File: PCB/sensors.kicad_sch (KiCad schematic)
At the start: 0 parts

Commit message: Added more components and added most needed values for the nrf example schematic
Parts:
- added J3: AudioJack4, symbol Connector_Audio:AudioJack4
- added U4: LTR-303ALS-01, OptoDevice:Lite-On_LTR-303ALS-01, symbol Sensor_Optical:LTR-303ALS-01
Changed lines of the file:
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@@
 	(generator_version "8.0")
 	(paper "A4")
+	(global_label "P0.07_EN_SENSOR_BUS"
+		(shape input)
+		(at 115.57 76.2 0)
+		(fields_autoplaced yes)
+		(effects
+			(font
+				(size 1.27 1.27)
+			)
+			(justify left)
+		)
+		(property "Intersheetrefs" "${INTERSHEET_REFS}"
+			(at 140.7498 76.2 0)
+			(effects
+				(font
+					(size 1.27 1.27)
+				)
+				(justify left)
+				(hide yes)
+			)
+		)
+	)
+	(global_label "P0.14_SCL"
+		(shape input)
+		(at 115.57 81.28 0)
+		(fields_autoplaced yes)
+		(effects
+			(font
+				(size 1.27 1.27)
+			)
+			(justify left)
+		)
+		(property "Intersheetrefs" "${INTERSHEET_REFS}"
+			(at 128.5337 81.28 0)
+			(effects
+				(font
+					(size 1.27 1.27)
+				)
+				(justify left)
+				(hide yes)
+			)
+		)
+	)
+	(global_label "P0.15_SDA"
+		(shape input)
+		(at 115.57 83.82 0)
+		(fields_autoplaced yes)
+		(effects
+			(font
+				(size 1.27 1.27)
+			)
+			(justify left)
+		)
+		(property "Intersheetrefs" "${INTERSHEET_REFS}"
+			(at 128.5942 83.82 0)
+			(effects
+				(font
+					(size 1.27 1.27)
+				)
+				(justify left)
+				(hide yes)
+			)
+		)
+	)
+	(symbol
+		(lib_id "Sensor_Optical:LTR-303ALS-01")
+		(at 203.2 91.44 0)
+		(unit 1)
+		(exclude_from_sim no)
+		(in_bom yes)
+		(on_board yes)
+		(dnp no)
+		(fields_autoplaced yes)
+		(property "Reference" "U4"
+			(at 219.71 85.1214 0)
+			(effects
+				(font
+					(size 1.27 1.27)
+				)
+			)
+		)
+		(property "Value" "LTR-303ALS-01"
+			(at 219.71 87.6614 0)
+			(effects
+				(font
+					(size 1.27 1.27)
+				)
+			)
+		)
+		(property "Footprint" "OptoDevice:Lite-On_LTR-303ALS-01"
+			(at 203.2 80.01 0)
+			(effects
+				(font
+					(size 1.27 1.27)
+				)
+				(hide yes)
+			)
+		)
+		(property "Datasheet" "https://optoelectronics.liteon.com/upload/download/DS86-2013-0004/LTR-303ALS-01_DS_V1.pdf"
+			(at 195.58 82.55 0)
+			(effects
+				(font
+					(size 1.27 1.27)
+				)
+				(hide yes)
+			)
+		)
+		(property "Description" "ambient light sensor, i2c interface, 0.01 to 64k lux, 2.4-3.6V"
+			(at 203.2 91.44 0)
+			(effects
+				(font
+					(size 1.27 1.27)
+				)
+				(hide yes)
+			)
+		)
+		(pin "1"
+		)
+		(pin "3"
+		)
+		(pin "4"
+		)
+		(pin "5"
+		)
+		(pin "6"
+		)
+		(pin "2"
+		)
+		(instances
+			(project "Plant_Thing"
+				(path "/3604ffe7-6852-4862-a71a-75c04c0147cb/38766e62-e2f9-438f-aa7f-b6d1382d0577"
+					(reference "U4")
+					(unit 1)
+				)
+			)
+		)
+	)
+	(symbol
+		(lib_id "Connector_Audio:AudioJack4")
+		(at 50.8 45.72 0)
+		(unit 1)
+		(exclude_from_sim no)
+		(in_bom yes)
+		(on_board yes)
+		(dnp no)
+		(fields_autoplaced yes)
+		(property "Reference" "J3"
+			(at 48.26 36.83 0)
+			(effects
+				(font
+					(size 1.27 1.27)
+				)
+			)
+		)
+		(property "Value" "AudioJack4"
+			(at 48.26 39.37 0)
+			(effects
+				(font
+					(size 1.27 1.27)
+				)
+			)
+		)
+		(property "Footprint" ""
+			(at 50.8 45.72 0)
+			(effects
+				(font
+					(size 1.27 1.27)
+				)
+				(hide yes)
+			)
+		)
+		(property "Datasheet" "~"
+			(at 50.8 45.72 0)
+			(effects
+				(font
+					(size 1.27 1.27)
+				)
+				(hide yes)
+			)
+		)
+		(property "Description" "Audio Jack, 4 Poles (TRRS)"
+			(at 50.8 45.72 0)
+			(effects
+				(font
+					(size 1.27 1.27)
+				)
+				(hide yes)
+			)
+		)
+		(pin "R1"
+		)
+		(pin "T"
+		)
+		(pin "S"
+		)
+		(pin "R2"
+		)
+		(instances
+			(project "Plant_Thing"
+				(path "/3604ffe7-6852-4862-a71a-75c04c0147cb/38766e62-e2f9-438f-aa7f-b6d1382d0577"
+					(reference "J3")
+					(unit 1)
+				)
+			)
+		)
+	)
 )

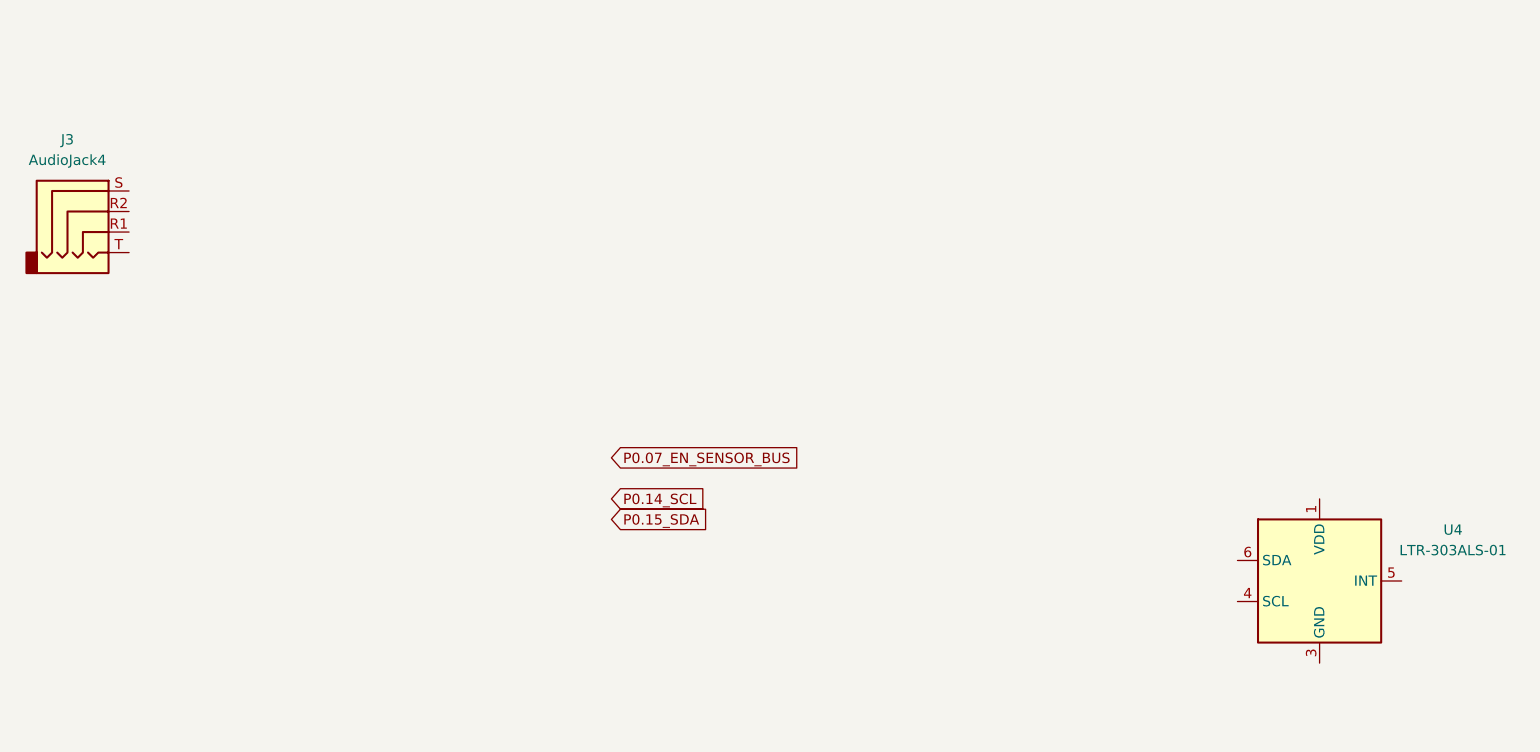
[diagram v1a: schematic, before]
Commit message: Added the Calathea Leaf as the outline and artwork for the project
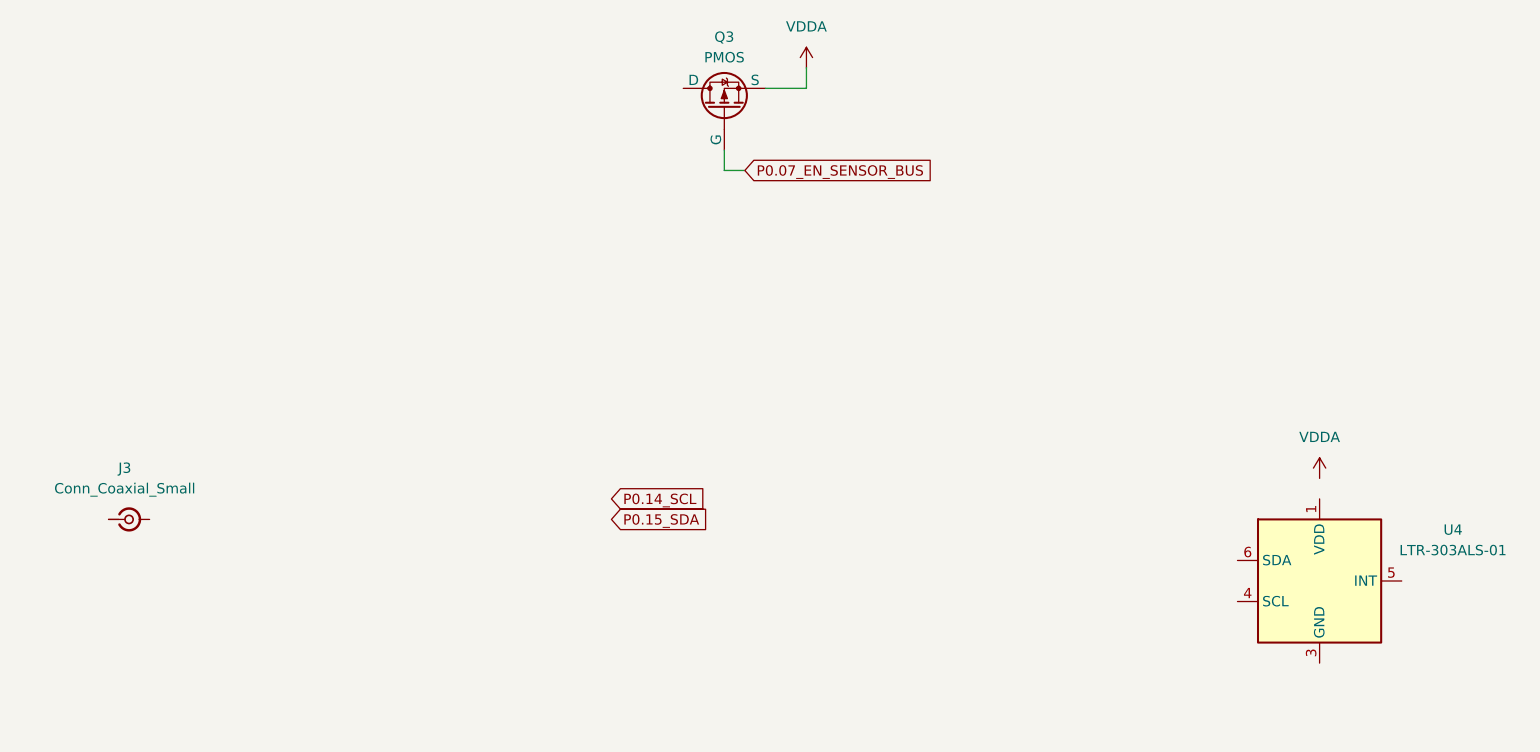
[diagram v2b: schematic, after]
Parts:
- removed J3: AudioJack4, symbol Connector_Audio:AudioJack4
- added J3: Conn_Coaxial_Small, Connector_Coaxial:SMA_Amphenol_132289_EdgeMount, symbol Connector:Conn_Coaxial_Small
- added Q3: PMOS, symbol Simulation_SPICE:PMOS
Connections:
- net P0.07_EN_SENSOR_BUS: now also Q3.2 (G)
- new net VDDA: Q3.3 (S)

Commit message: added dcdc for external components. Changed board edge to a rect for easier dev board routuing.
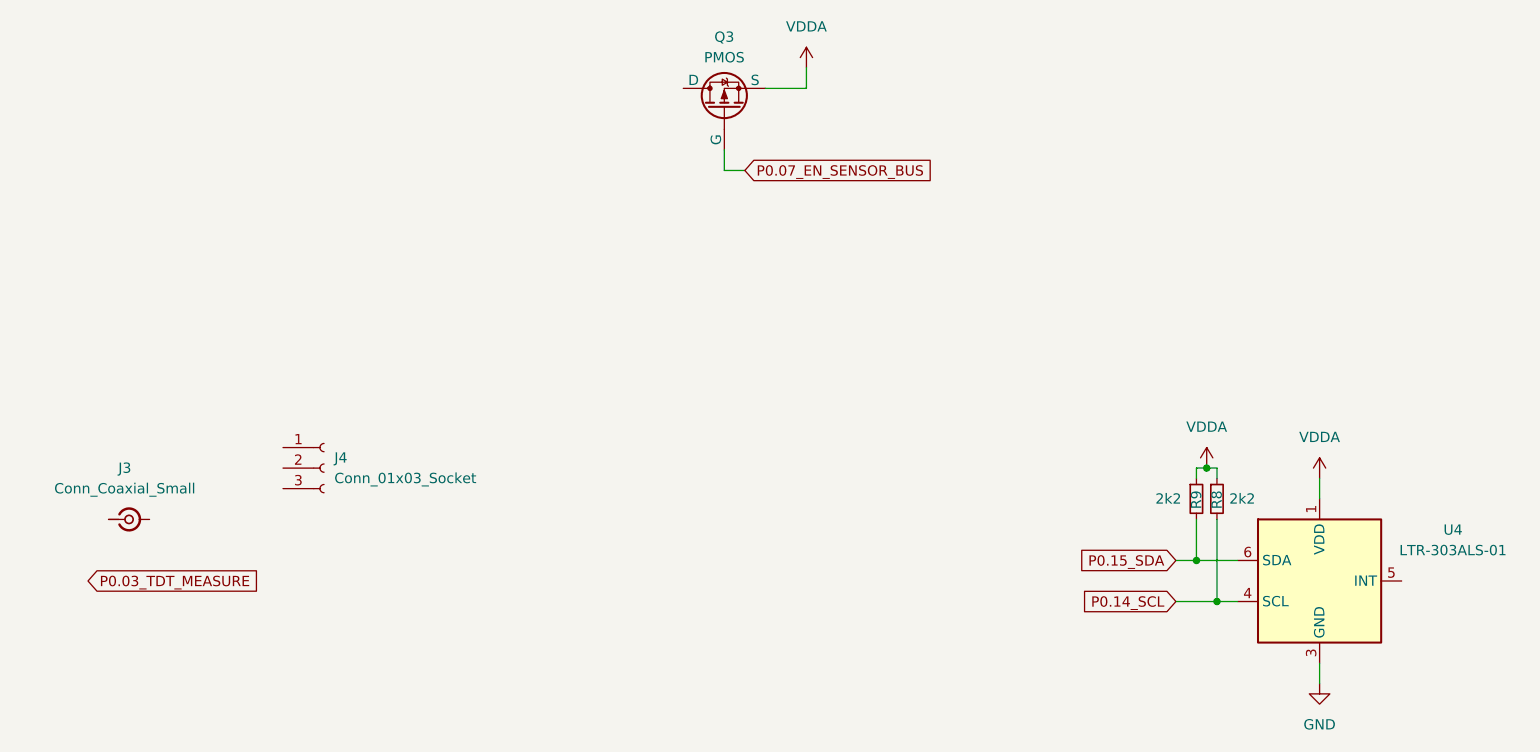
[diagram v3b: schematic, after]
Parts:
- added J4: Conn_01x03_Socket, Connector_PinSocket_2.54mm:PinSocket_1x03_P2.54mm_Horizontal, symbol Connector:Conn_01x03_Socket
- added R8, R9: 2k2, Resistor_SMD:R_0402_1005Metric, symbol Device:R_Small
- J3: footprint Connector_Coaxial:SMA_Amphenol_132289_EdgeMount -> Connector_Coaxial:U.FL_Molex_MCRF_73412-0110_Vertical
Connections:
- net P0.14_SCL: now also U4.4 (SCL), R8.2
- net P0.15_SDA: now also U4.6 (SDA), R9.2
- net VDDA: now also U4.1 (VDD), R8.1, R9.1
- net GND: now reaches U4.3 (GND)

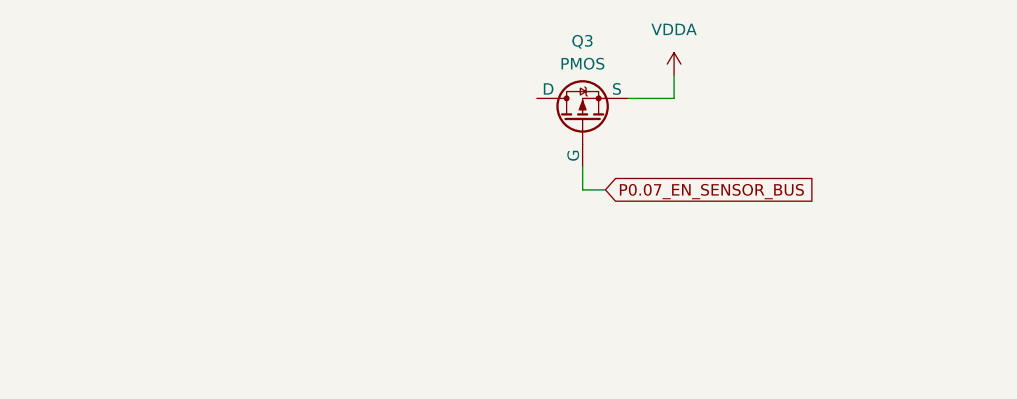
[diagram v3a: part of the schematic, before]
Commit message: redid the pcb layout for a more bigger devboard approach. Added a few more components and the antenna.
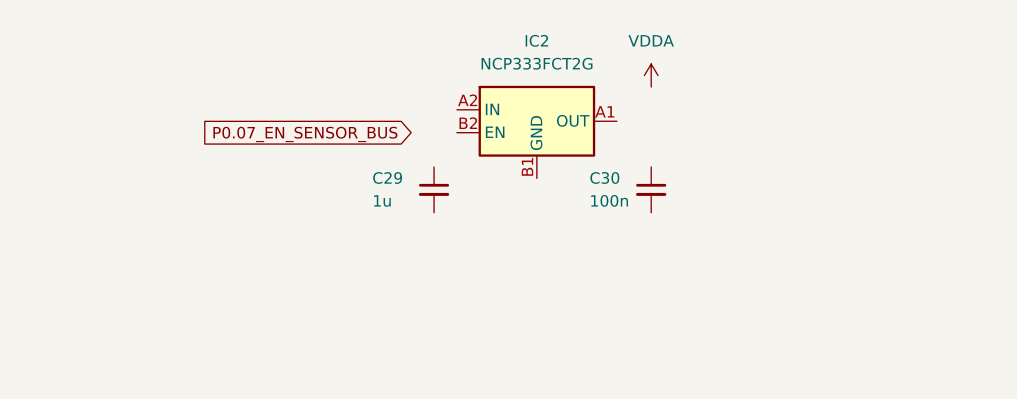
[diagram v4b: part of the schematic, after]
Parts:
- removed Q3: PMOS, symbol Simulation_SPICE:PMOS
- added C29: 1u, Capacitor_SMD:C_0402_1005Metric, symbol Device:C_Small
- added C30: 100n, Capacitor_SMD:C_0402_1005Metric, symbol Device:C_Small
- added IC2: NCP333FCT2G, BGA4C40P2X2_76X76X63, symbol NCP333FCT2G:NCP333FCT2G

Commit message: Added more Components
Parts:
- added J6: TDT, Connector_PinHeader_2.54mm:PinHeader_1x02_P2.54mm_Vertical, symbol Connector:Conn_01x02_Pin
- added TP13, TP3, TP4: TestPoint_Small, TestPoint:TestPoint_Pad_D1.0mm, symbol Connector:TestPoint_Small
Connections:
- net GND: now also C29.2, C30.2, IC2.B1 (GND)
- net P0.07_EN_SENSOR_BUS: now also IC2.B2 (EN)
- net P0.14_SCL: now also TP3.1
- net P0.15_SDA: now also TP4.1
- net VDDA: now also C30.1, IC2.A1 (OUT)
- net at U4.5 (INT): now also TP13.1
- net +3.3V: now reaches IC2.A2 (IN)
- net +3.3V: now also C29.1
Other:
- moved on the sheet: C30

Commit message: Continued on Devboard
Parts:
- removed J3: Conn_Coaxial_Small, Connector_Coaxial:U.FL_Molex_MCRF_73412-0110_Vertical, symbol Connector:Conn_Coaxial_Small
- removed J4: Conn_01x03_Socket, Connector_PinSocket_2.54mm:PinSocket_1x03_P2.54mm_Horizontal, symbol Connector:Conn_01x03_Socket
- added J3: Conn_01x06_Pin, Connector_PinHeader_2.54mm:PinHeader_1x06_P2.54mm_Vertical, symbol Connector:Conn_01x06_Pin
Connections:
- net GND: now also J3.1 (Pin_1), J3.3 (Pin_3), J3.5 (Pin_5)
- net P0.03_TDT_MEASURE: now also J3.2 (Pin_2)
- net P0.04_AGPIO: now also J3.4 (Pin_4)
- net VDDA: now also J6.1 (Pin_1)
- net at J6.2 (Pin_2): now also J3.6 (Pin_6)
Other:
- moved on the sheet: J6

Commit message: Finished Devboard
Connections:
- net GND: no longer J3.3 (Pin_3)
- net P0.04_AGPIO renamed P0.05_AIN3
- new net P0.04_AIN2: J3.3 (Pin_3)
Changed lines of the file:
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@@
+		)
+	)
+	(global_label "P0.04_AIN2"
+		(shape input)
+		(at 92.71 95.25 0)
+		(fields_autoplaced yes)
+		(effects
+			(font
+				(size 1.27 1.27)
+			)
+			(justify left)
+		)
+		(property "Intersheetrefs" "${INTERSHEET_REFS}"
+			(at 106.3995 95.25 0)
+			(effects
+				(font
+					(size 1.27 1.27)
+				)
+				(justify left)
+				(hide yes)
+			)
 		)
 	)
@@
 		)
 	)
-	(global_label "P0.04_AGPIO"
+	(global_label "P0.05_AIN3"
 		(shape input)
 		(at 92.71 92.71 0)
@@
 		)
 		(property "Intersheetrefs" "${INTERSHEET_REFS}"
-			(at 107.73 92.71 0)
+			(at 106.3995 92.71 0)
 			(effects
 				(font
@@
 					(unit 1)
 				)
-			)
-		)
-	)
-	(symbol
-		(lib_id "power:GND")
-		(at 92.71 95.25 90)
-		(mirror x)
-		(unit 1)
-		(exclude_from_sim no)
-		(in_bom yes)
-		(on_board yes)
-		(dnp no)
-		(fields_autoplaced yes)
-		(property "Reference" "#PWR070"
-			(at 99.06 95.25 0)
-			(effects
-				(font
-					(size 1.27 1.27)
-				)
-				(hide yes)
-			)
-		)
-		(property "Value" "GND"
-			(at 96.52 95.2501 90)
-			(effects
-				(font
-					(size 1.27 1.27)
-				)
-				(justify right)
-			)
-		)
-		(property "Footprint" ""
-			(at 92.71 95.25 0)
-			(effects
-				(font
-					(size 1.27 1.27)
-				)
-				(hide yes)
-			)
-		)
-		(property "Datasheet" ""
-			(at 92.71 95.25 0)
-			(effects
-				(font
-					(size 1.27 1.27)
-				)
-				(hide yes)
-			)
-		)
-		(property "Description" "Power symbol creates a global label with name \"GND\" , ground"
-			(at 92.71 95.25 0)
-			(effects
-				(font
-					(size 1.27 1.27)
-				)
-				(hide yes)
-			)
-		)
-		(pin "1"
-		)
-		(instances
-			(project "Plant_Thing"
-				(path "/3604ffe7-6852-4862-a71a-75c04c0147cb/38766e62-e2f9-438f-aa7f-b6d1382d0577"
-					(reference "#PWR070")
-					(unit 1)
-				)
